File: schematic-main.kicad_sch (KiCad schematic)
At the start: 16 parts, among them J1 Battery, J2 CAN, J3 V_P, J6 MOTOR_DRIVER, J7 C_P, J8 VALVE, J9 PURGE_VALVE, P1 USB_C_Plug_USB2.0

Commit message: Change of dimensions
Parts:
- removed J6: MOTOR_DRIVER, Connector_Molex:Molex_KK-396_A-41792-0003_1x03_P3.96mm_Horizontal, symbol Connector_Generic:Conn_01x03
- added J10: Motor, Connector_Molex:Molex_KK-396_A-41791-0002_1x02_P3.96mm_Vertical, symbol Connector_Generic:Conn_01x02
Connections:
- net IO_2/+MOTOR: now also J10.1 (Pin_1)
- net IO_2/-MOTOR: now also J10.2 (Pin_2)
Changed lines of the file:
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@@
-	(wire
-		(pts
-			(xy 236.22 140.97) (xy 236.22 139.7)
-		)
-		(stroke
-			(width 0)
-			(type default)
-		)
-	)
 	(wire
 		(pts
@@
 	)
 	(symbol
-		(lib_id "Connector_Generic:Conn_01x03")
-		(at 231.14 137.16 0)
-		(mirror y)
-		(unit 1)
-		(exclude_from_sim no)
-		(in_bom yes)
-		(on_board yes)
-		(dnp no)
-		(property "Reference" "J6"
-			(at 225.552 146.558 90)
-			(effects
-				(font
-					(size 1.27 1.27)
-				)
-				(justify left)
-			)
-		)
-		(property "Value" "MOTOR_DRIVER"
-			(at 228.092 146.558 90)
-			(effects
-				(font
-					(size 1.27 1.27)
-				)
-				(justify left)
-			)
-		)
-		(property "Footprint" "Connector_Molex:Molex_KK-396_A-41792-0003_1x03_P3.96mm_Horizontal"
-			(at 231.14 137.16 0)
-			(effects
-				(font
-					(size 1.27 1.27)
-				)
-				(hide yes)
-			)
-		)
-		(property "Datasheet" "~"
-			(at 231.14 137.16 0)
-			(effects
-				(font
-					(size 1.27 1.27)
-				)
-				(hide yes)
-			)
-		)
-		(property "Description" ""
-			(at 231.14 137.16 0)
-			(effects
-				(font
-					(size 1.27 1.27)
-				)
-				(hide yes)
-			)
-		)
-		(pin "1"
-		)
-		(pin "2"
-		)
-		(pin "3"
-		)
-		(instances
-			(project "schematic-main"
-				(path "/c9ad7189-d3b2-414a-9743-efd8e57cd755"
-					(reference "J6")
-					(unit 1)
-				)
-			)
-		)
-	)
-	(symbol
 		(lib_id "Connector_Generic:Conn_01x02")
 		(at 125.73 144.526 180)
@@
 	)
 	(symbol
-		(lib_id "power:GND")
-		(at 236.22 140.97 0)
-		(unit 1)
-		(exclude_from_sim no)
-		(in_bom yes)
-		(on_board yes)
-		(dnp no)
-		(fields_autoplaced yes)
-		(property "Reference" "#PWR079"
-			(at 236.22 147.32 0)
-			(effects
-				(font
-					(size 1.27 1.27)
-				)
-				(hide yes)
-			)
-		)
-		(property "Value" "GND"
-			(at 236.22 146.05 0)
-			(effects
-				(font
-					(size 1.27 1.27)
-				)
-				(hide yes)
-			)
-		)
-		(property "Footprint" ""
-			(at 236.22 140.97 0)
-			(effects
-				(font
-					(size 1.27 1.27)
-				)
-				(hide yes)
-			)
-		)
-		(property "Datasheet" ""
-			(at 236.22 140.97 0)
-			(effects
-				(font
-					(size 1.27 1.27)
-				)
-				(hide yes)
-			)
-		)
-		(property "Description" ""
-			(at 236.22 140.97 0)
+		(lib_id "Connector_Generic:Conn_01x02")
+		(at 231.14 137.16 180)
+		(unit 1)
+		(exclude_from_sim no)
+		(in_bom yes)
+		(on_board yes)
+		(dnp no)
+		(property "Reference" "J10"
+			(at 225.298 135.89 90)
+			(effects
+				(font
+					(size 1.27 1.27)
+				)
+			)
+		)
+		(property "Value" "Motor"
+			(at 227.838 135.89 90)
+			(effects
+				(font
+					(size 1.27 1.27)
+				)
+			)
+		)
+		(property "Footprint" "Connector_Molex:Molex_KK-396_A-41791-0002_1x02_P3.96mm_Vertical"
+			(at 231.14 137.16 0)
+			(effects
+				(font
+					(size 1.27 1.27)
+				)
+				(hide yes)
+			)
+		)
+		(property "Datasheet" "~"
+			(at 231.14 137.16 0)
+			(effects
+				(font
+					(size 1.27 1.27)
+				)
+				(hide yes)
+			)
+		)
+		(property "Description" ""
+			(at 231.14 137.16 0)
 			(effects
 				(font
@@
 		(pin "1"
 		)
-		(instances
-			(project "schematic-main"
-				(path "/c9ad7189-d3b2-414a-9743-efd8e57cd755"
-					(reference "#PWR079")
-					(unit 1)
-				)
+		(pin "2"
+		)
+		(instances
+			(project "schematic-main"
+				(path "/c9ad7189-d3b2-414a-9743-efd8e57cd755"
+					(reference "J10")
+					(unit 1)
+				)

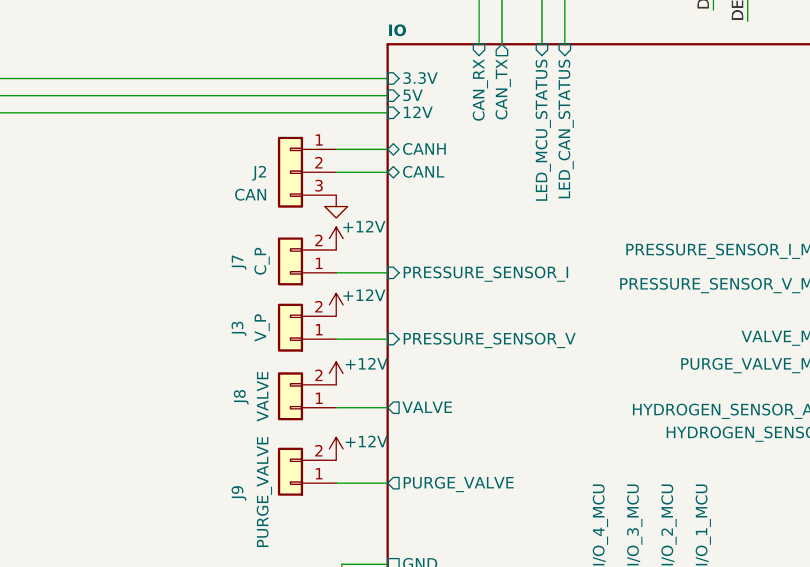
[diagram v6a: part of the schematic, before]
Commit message: Change presure sensor socket
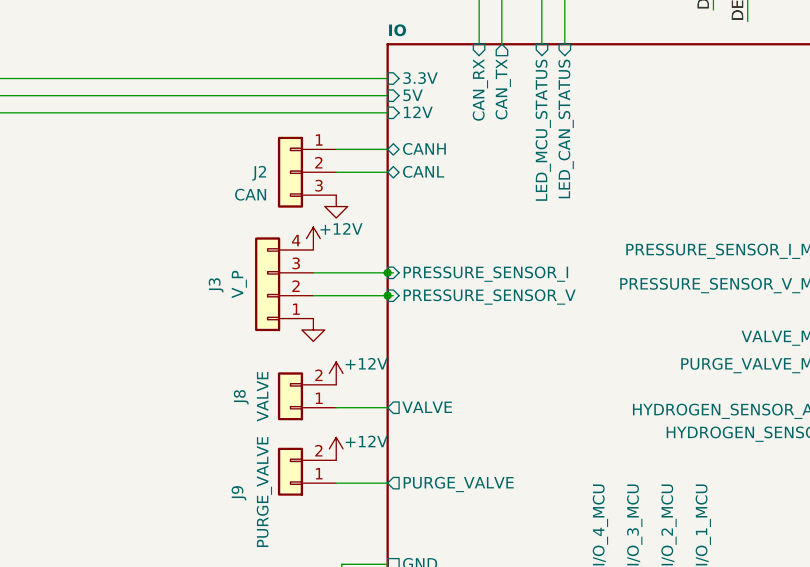
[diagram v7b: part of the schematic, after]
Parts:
- removed J3: V_P, Connector_Molex:39-30-102Y, symbol Connector_Generic:Conn_01x02
- removed J7: C_P, Connector_Molex:39-30-102Y, symbol Connector_Generic:Conn_01x02
- added J3: V_P, Lib:39-30-104Y, symbol Connector_Generic:Conn_01x04
- J10: footprint Connector_Molex:Molex_KK-396_A-41791-0002_1x02_P3.96mm_Vertical -> Connector_Molex:39-30-102Y
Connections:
- net +12V: now also J3.4 (Pin_4)
- net GND: now also J3.1 (Pin_1)
- net IO/PRESSURE_SENSOR_I: now also J3.3 (Pin_3)
- net IO/PRESSURE_SENSOR_V: now also J3.2 (Pin_2)
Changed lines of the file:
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@@
 	)
 	(junction
+		(at 136.525 129.54)
+		(diameter 0)
+		(color 0 0 0 0)
+	)
+	(junction
 		(at 34.29 34.29)
 		(diameter 0)
@@
 	)
 	(junction
+		(at 136.525 132.08)
+		(diameter 0)
+		(color 0 0 0 0)
+	)
+	(junction
 		(at 96.52 85.09)
 		(diameter 0)
@@
 	(wire
 		(pts
-			(xy 130.81 136.906) (xy 136.525 136.906)
-		)
-		(stroke
-			(width 0)
-			(type default)
-		)
-	)
-	(wire
-		(pts
 			(xy 187.96 144.78) (xy 212.09 144.78)
 		)
@@
 	(wire
 		(pts
+			(xy 128.27 129.54) (xy 136.525 129.54)
+		)
+		(stroke
+			(width 0)
+			(type default)
+		)
+	)
+	(wire
+		(pts
 			(xy 168.91 81.28) (xy 168.91 96.52)
 		)
@@
 	(wire
 		(pts
+			(xy 136.525 129.54) (xy 137.16 129.54)
+		)
+		(stroke
+			(width 0)
+			(type default)
+		)
+	)
+	(wire
+		(pts
 			(xy 76.2 29.21) (xy 76.2 33.02)
 		)
@@
 	(wire
 		(pts
-			(xy 130.81 129.54) (xy 136.525 129.54)
-		)
-		(stroke
-			(width 0)
-			(type default)
-		)
-	)
-	(wire
-		(pts
 			(xy 222.25 119.38) (xy 241.3 119.38)
 		)
@@
 	(wire
 		(pts
+			(xy 128.27 132.08) (xy 136.525 132.08)
+		)
+		(stroke
+			(width 0)
+			(type default)
+		)
+	)
+	(wire
+		(pts
 			(xy 131.445 161.925) (xy 131.445 163.83)
 		)
@@
 	(wire
 		(pts
+			(xy 136.525 132.08) (xy 137.16 132.08)
+		)
+		(stroke
+			(width 0)
+			(type default)
+		)
+	)
+	(wire
+		(pts
 			(xy 123.19 54.61) (xy 136.525 54.61)
 		)
@@
 	)
 	(symbol
-		(lib_id "Connector_Generic:Conn_01x02")
-		(at 125.73 129.54 180)
-		(unit 1)
-		(exclude_from_sim no)
-		(in_bom yes)
-		(on_board yes)
-		(dnp no)
-		(property "Reference" "J7"
-			(at 119.888 128.27 90)
-			(effects
-				(font
-					(size 1.27 1.27)
-				)
-			)
-		)
-		(property "Value" "C_P"
-			(at 122.428 128.27 90)
-			(effects
-				(font
-					(size 1.27 1.27)
-				)
-			)
-		)
-		(property "Footprint" "Connector_Molex:39-30-102Y"
-			(at 125.73 129.54 0)
-			(effects
-				(font
-					(size 1.27 1.27)
-				)
-				(hide yes)
-			)
-		)
-		(property "Datasheet" "~"
-			(at 125.73 129.54 0)
-			(effects
-				(font
-					(size 1.27 1.27)
-				)
-				(hide yes)
-			)
-		)
-		(property "Description" ""
-			(at 125.73 129.54 0)
-			(effects
-				(font
-					(size 1.27 1.27)
-				)
-				(hide yes)
-			)
-		)
-		(pin "1"
-		)
-		(pin "2"
-		)
-		(instances
-			(project "schematic-main"
-				(path "/c9ad7189-d3b2-414a-9743-efd8e57cd755"
-					(reference "J7")
-					(unit 1)
-				)
-			)
-		)
-	)
-	(symbol
 		(lib_id "Connector:USB_C_Plug_USB2.0")
 		(at 96.52 60.96 0)
@@
 	)
 	(symbol
-		(lib_id "power:+12V")
-		(at 130.81 127 0)
-		(unit 1)
-		(exclude_from_sim no)
-		(in_bom yes)
-		(on_board yes)
-		(dnp no)
-		(property "Reference" "#PWR060"
-			(at 130.81 130.81 0)
-			(effects
-				(font
-					(size 1.27 1.27)
-				)
-				(hide yes)
-			)
-		)
-		(property "Value" "+12V"
-			(at 133.858 124.46 0)
-			(effects
-				(font
-					(size 1.27 1.27)
-				)
-			)
-		)
-		(property "Footprint" ""
-			(at 130.81 127 0)
-			(effects
-				(font
-					(size 1.27 1.27)
-				)
-				(hide yes)
-			)
-		)
-		(property "Datasheet" ""
-			(at 130.81 127 0)
-			(effects
-				(font
-					(size 1.27 1.27)
-				)
-				(hide yes)
-			)
-		)
-		(property "Description" ""
-			(at 130.81 127 0)
-			(effects
-				(font
-					(size 1.27 1.27)
-				)
-				(hide yes)
-			)
-		)
-		(pin "1"
-		)
-		(instances
-			(project "schematic-main"
-				(path "/c9ad7189-d3b2-414a-9743-efd8e57cd755"
-					(reference "#PWR060")
-					(unit 1)
-				)
-			)
-		)
-	)
-	(symbol
 		(lib_id "Connector_Generic:Conn_01x02")
 		(at 125.73 152.908 180)
@@
 	)
 	(symbol
-		(lib_id "Connector_Generic:Conn_01x02")
-		(at 125.73 136.906 180)
+		(lib_id "Connector_Generic:Conn_01x04")
+		(at 123.19 132.08 180)
 		(unit 1)
 		(exclude_from_sim no)
@@
 		(dnp no)
 		(property "Reference" "J3"
-			(at 119.888 135.636 90)
+			(at 117.348 130.81 90)
 			(effects
 				(font
@@
 		)
 		(property "Value" "V_P"
-			(at 122.428 135.636 90)
+			(at 119.888 130.81 90)
 			(effects
 				(font
@@
 			)
 		)
-		(property "Footprint" "Connector_Molex:39-30-102Y"
-			(at 125.73 136.906 0)
+		(property "Footprint" "Lib:39-30-104Y"
+			(at 123.19 132.08 0)
 			(effects
 				(font
@@
 		)
 		(property "Datasheet" "~"
-			(at 125.73 136.906 0)
+			(at 123.19 132.08 0)
 			(effects
 				(font
@@
 			)
 		)
-		(property "Description" ""
-			(at 125.73 136.906 0)
+		(property "Description" "Generic connector, single row, 01x04, script generated (kicad-library-utils/schlib/autogen/connector/)"
+			(at 123.19 132.08 0)
 			(effects
 				(font
@@
 		(pin "2"
 		)
+		(pin "3"
+		)
+		(pin "4"
+		)
 		(instances
 			(project "schematic-main"
@@
 	(symbol
 		(lib_id "power:+12V")
-		(at 130.81 134.366 0)
+		(at 128.27 127 0)
 		(unit 1)
 		(exclude_from_sim no)
@@
 		(dnp no)
 		(property "Reference" "#PWR061"
-			(at 130.81 138.176 0)
+			(at 128.27 130.81 0)
 			(effects
 				(font
@@
 		)
 		(property "Value" "+12V"
-			(at 133.858 132.08 0)
+			(at 131.318 124.714 0)
 			(effects
 				(font
@@
 		)
 		(property "Footprint" ""
-			(at 130.81 134.366 0)
+			(at 128.27 127 0)
 			(effects
 				(font
@@
 		)
 		(property "Datasheet" ""
-			(at 130.81 134.366 0)
+			(at 128.27 127 0)
 			(effects
 				(font
@@
 		)
 		(property "Description" ""
-			(at 130.81 134.366 0)
+			(at 128.27 127 0)
 			(effects
 				(font
@@
 	)
 	(symbol
+		(lib_id "power:GND")
+		(at 128.27 134.62 0)
+		(unit 1)
+		(exclude_from_sim no)
+		(in_bom yes)
+		(on_board yes)
+		(dnp no)
+		(fields_autoplaced yes)
+		(property "Reference" "#PWR060"
+			(at 128.27 140.97 0)
+			(effects
+				(font
+					(size 1.27 1.27)
+				)
+				(hide yes)
+			)
+		)
+		(property "Value" "GND"
+			(at 128.27 139.7 0)
+			(effects
+				(font
+					(size 1.27 1.27)
+				)
+				(hide yes)
+			)
+		)
+		(property "Footprint" ""
+			(at 128.27 134.62 0)
+			(effects
+				(font
+					(size 1.27 1.27)
+				)
+				(hide yes)
+			)
+		)
+		(property "Datasheet" ""
+			(at 128.27 134.62 0)
+			(effects
+				(font
+					(size 1.27 1.27)
+				)
+				(hide yes)
+			)
+		)
+		(property "Description" ""
+			(at 128.27 134.62 0)
+			(effects
+				(font
+					(size 1.27 1.27)
+				)
+				(hide yes)
+			)
+		)
+		(pin "1"
+		)
+		(instances
+			(project "schematic-main"
+				(path "/c9ad7189-d3b2-414a-9743-efd8e57cd755"
+					(reference "#PWR060")
+					(unit 1)
+				)
+			)
+		)
+	)
+	(symbol
 		(lib_id "Mechanical:MountingHole")
 		(at 36.83 131.699 0)
@@
 			)
 		)
-		(property "Footprint" "Connector_Molex:Molex_KK-396_A-41791-0002_1x02_P3.96mm_Vertical"
+		(property "Footprint" "Connector_Molex:39-30-102Y"
 			(at 231.14 137.16 0)
 			(effects
@@
 		)
 		(pin "PRESSURE_SENSOR_V" input
-			(at 136.525 136.906 180)
+			(at 136.525 132.08 180)
 			(effects
 				(font
